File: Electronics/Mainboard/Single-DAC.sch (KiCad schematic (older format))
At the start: 21 parts, among them U10 AD8675, U5 AD5781, U9 AD8676xR

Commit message: Mainboard layout and schematic done
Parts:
- C26, C71, C72: LCSC (none) -> C1634
- C26, C27, C29, C30, C31, C32, C37: LCSC (none) -> C14663
- C32, C35, C36, C39, C40, C43, C44: LCSC (none) -> C15850
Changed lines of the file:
@@
 $Descr A4 11693 8268
 encoding utf-8
-Sheet 6 11
+Sheet 10 11
 Title ""
 Date ""
@@
 F 2 "Capacitor_SMD:C_0603_1608Metric_Pad1.05x0.95mm_HandSolder" H 6238 3350 50  0001 C CNN
 F 3 "~" H 6200 3500 50  0001 C CNN
+F 4 "C1634" H 6200 3500 50  0001 C CNN "LCSC"
 	1    6200 3500
 	1    0    0    -1
@@
 F 2 "Capacitor_SMD:C_0805_2012Metric_Pad1.15x1.40mm_HandSolder" H 9388 3950 50  0001 C CNN
 F 3 "~" H 9350 4100 50  0001 C CNN
+F 4 "C15850" H 9350 4100 50  0001 C CNN "LCSC"
 	1    9350 4100
 	1    0    0    -1
@@
 F 2 "Capacitor_SMD:C_0603_1608Metric_Pad1.05x0.95mm_HandSolder" H 8488 1950 50  0001 C CNN
 F 3 "~" H 8450 2100 50  0001 C CNN
+F 4 "C14663" H 8450 2100 50  0001 C CNN "LCSC"
 	1    8450 2100
 	1    0    0    -1
@@
 F 2 "Capacitor_SMD:C_0805_2012Metric_Pad1.15x1.40mm_HandSolder" H 8238 1950 50  0001 C CNN
 F 3 "~" H 8200 2100 50  0001 C CNN
+F 4 "C15850" H 8200 2100 50  0001 C CNN "LCSC"
 	1    8200 2100
 	1    0    0    -1
@@
 F 2 "Capacitor_SMD:C_0805_2012Metric_Pad1.15x1.40mm_HandSolder" H 8238 2450 50  0001 C CNN
 F 3 "~" H 8200 2600 50  0001 C CNN
+F 4 "C15850" H 8200 2600 50  0001 C CNN "LCSC"
 	1    8200 2600
 	1    0    0    -1
@@
 F 2 "Capacitor_SMD:C_0805_2012Metric_Pad1.15x1.40mm_HandSolder" H 8738 1950 50  0001 C CNN
 F 3 "~" H 8700 2100 50  0001 C CNN
+F 4 "C15850" H 8700 2100 50  0001 C CNN "LCSC"
 	1    8700 2100
 	1    0    0    -1
@@
 F 2 "Capacitor_SMD:C_0805_2012Metric_Pad1.15x1.40mm_HandSolder" H 8738 2450 50  0001 C CNN
 F 3 "~" H 8700 2600 50  0001 C CNN
+F 4 "C15850" H 8700 2600 50  0001 C CNN "LCSC"
 	1    8700 2600
 	1    0    0    -1
@@
 F 2 "Capacitor_SMD:C_0805_2012Metric_Pad1.15x1.40mm_HandSolder" H 9238 1950 50  0001 C CNN
 F 3 "~" H 9200 2100 50  0001 C CNN
+F 4 "C15850" H 9200 2100 50  0001 C CNN "LCSC"
 	1    9200 2100
 	1    0    0    -1
@@
 F 2 "Capacitor_SMD:C_0805_2012Metric_Pad1.15x1.40mm_HandSolder" H 9238 2450 50  0001 C CNN
 F 3 "~" H 9200 2600 50  0001 C CNN
+F 4 "C15850" H 9200 2600 50  0001 C CNN "LCSC"
 	1    9200 2600
 	1    0    0    -1
@@
 F 2 "Capacitor_SMD:C_0603_1608Metric_Pad1.05x0.95mm_HandSolder" H 8488 2450 50  0001 C CNN
 F 3 "~" H 8450 2600 50  0001 C CNN
+F 4 "C14663" H 8450 2600 50  0001 C CNN "LCSC"
 	1    8450 2600
 	1    0    0    -1
@@
 F 2 "Capacitor_SMD:C_0603_1608Metric_Pad1.05x0.95mm_HandSolder" H 8988 2450 50  0001 C CNN
 F 3 "~" H 8950 2600 50  0001 C CNN
+F 4 "C14663" H 8950 2600 50  0001 C CNN "LCSC"
 	1    8950 2600
 	1    0    0    -1
@@
 F 2 "Capacitor_SMD:C_0603_1608Metric_Pad1.05x0.95mm_HandSolder" H 8988 1950 50  0001 C CNN
 F 3 "~" H 8950 2100 50  0001 C CNN
+F 4 "C14663" H 8950 2100 50  0001 C CNN "LCSC"
 	1    8950 2100
 	1    0    0    -1
@@
 F 2 "Capacitor_SMD:C_0603_1608Metric_Pad1.05x0.95mm_HandSolder" H 9488 1950 50  0001 C CNN
 F 3 "~" H 9450 2100 50  0001 C CNN
+F 4 "C14663" H 9450 2100 50  0001 C CNN "LCSC"
 	1    9450 2100
 	1    0    0    -1
@@
 F 2 "Capacitor_SMD:C_0603_1608Metric_Pad1.05x0.95mm_HandSolder" H 9488 2450 50  0001 C CNN
 F 3 "~" H 9450 2600 50  0001 C CNN
+F 4 "C14663" H 9450 2600 50  0001 C CNN "LCSC"
 	1    9450 2600
 	1    0    0    -1
@@
 F 2 "Capacitor_SMD:C_0603_1608Metric_Pad1.05x0.95mm_HandSolder" H 9638 3950 50  0001 C CNN
 F 3 "~" H 9600 4100 50  0001 C CNN
+F 4 "C14663" H 9600 4100 50  0001 C CNN "LCSC"
 	1    9600 4100
 	1    0    0    -1
@@
 F 2 "Capacitor_SMD:C_0603_1608Metric_Pad1.05x0.95mm_HandSolder" H 4838 2150 50  0001 C CNN
 F 3 "~" H 4800 2300 50  0001 C CNN
+F 4 "C1634" H 4800 2300 50  0001 C CNN "LCSC"
 	1    4800 2300
 	1    0    0    -1
@@
 F 2 "Capacitor_SMD:C_0603_1608Metric_Pad1.05x0.95mm_HandSolder" H 4838 5000 50  0001 C CNN
 F 3 "~" H 4800 5150 50  0001 C CNN
+F 4 "C1634" H 4800 5150 50  0001 C CNN "LCSC"
 	1    4800 5150
 	1    0    0    -1

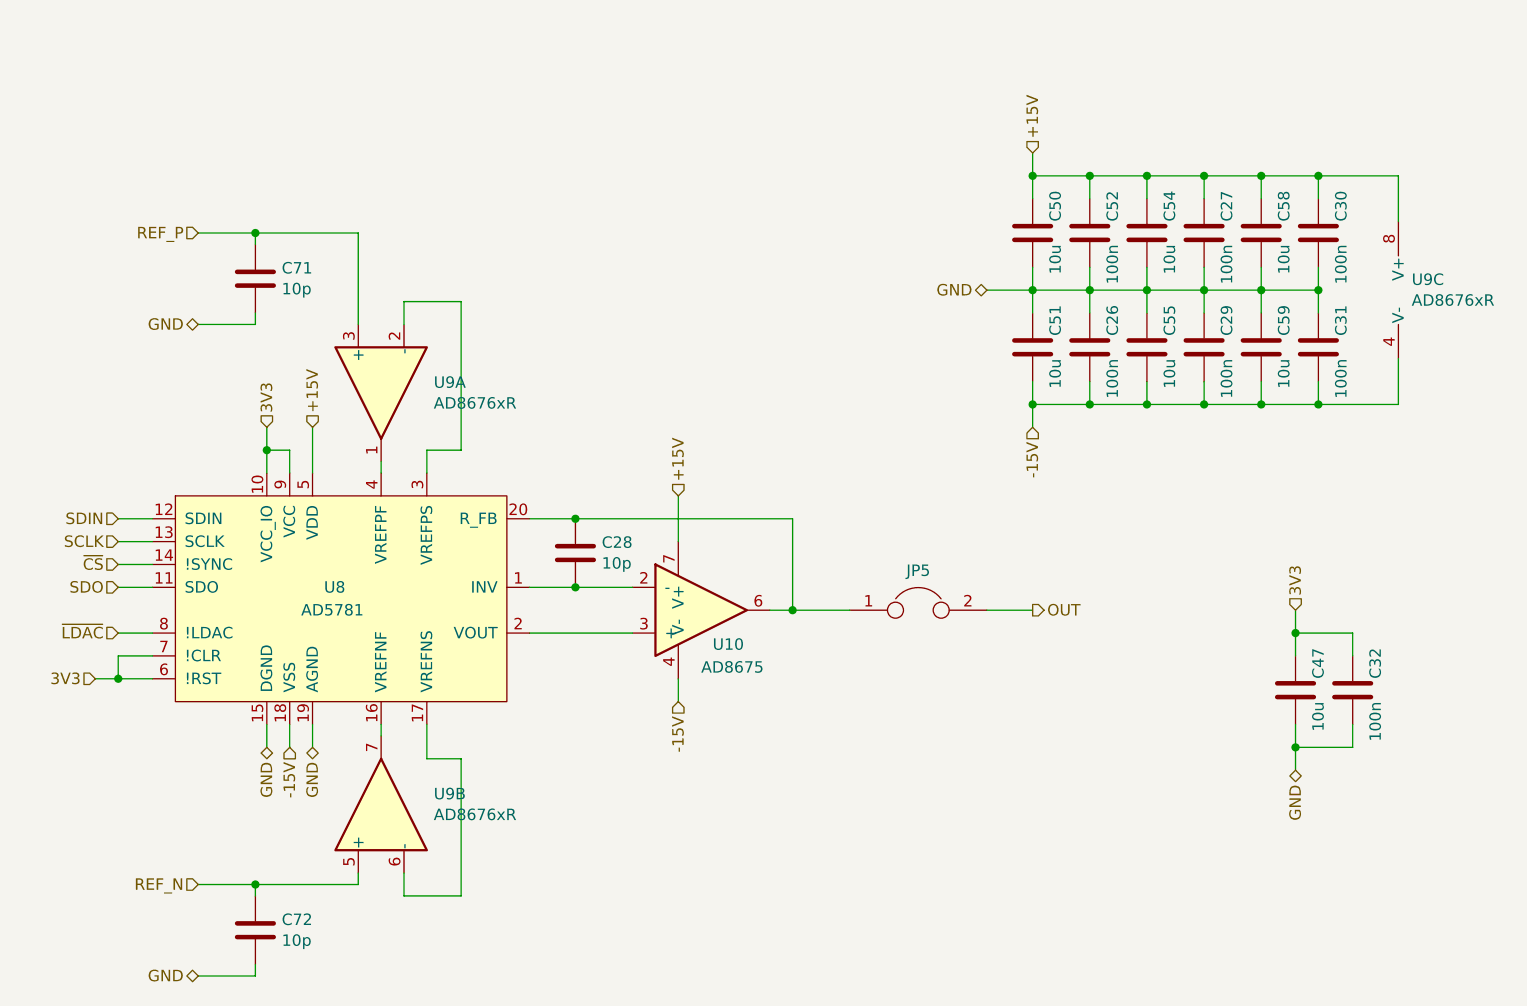
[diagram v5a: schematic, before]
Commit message: Added images
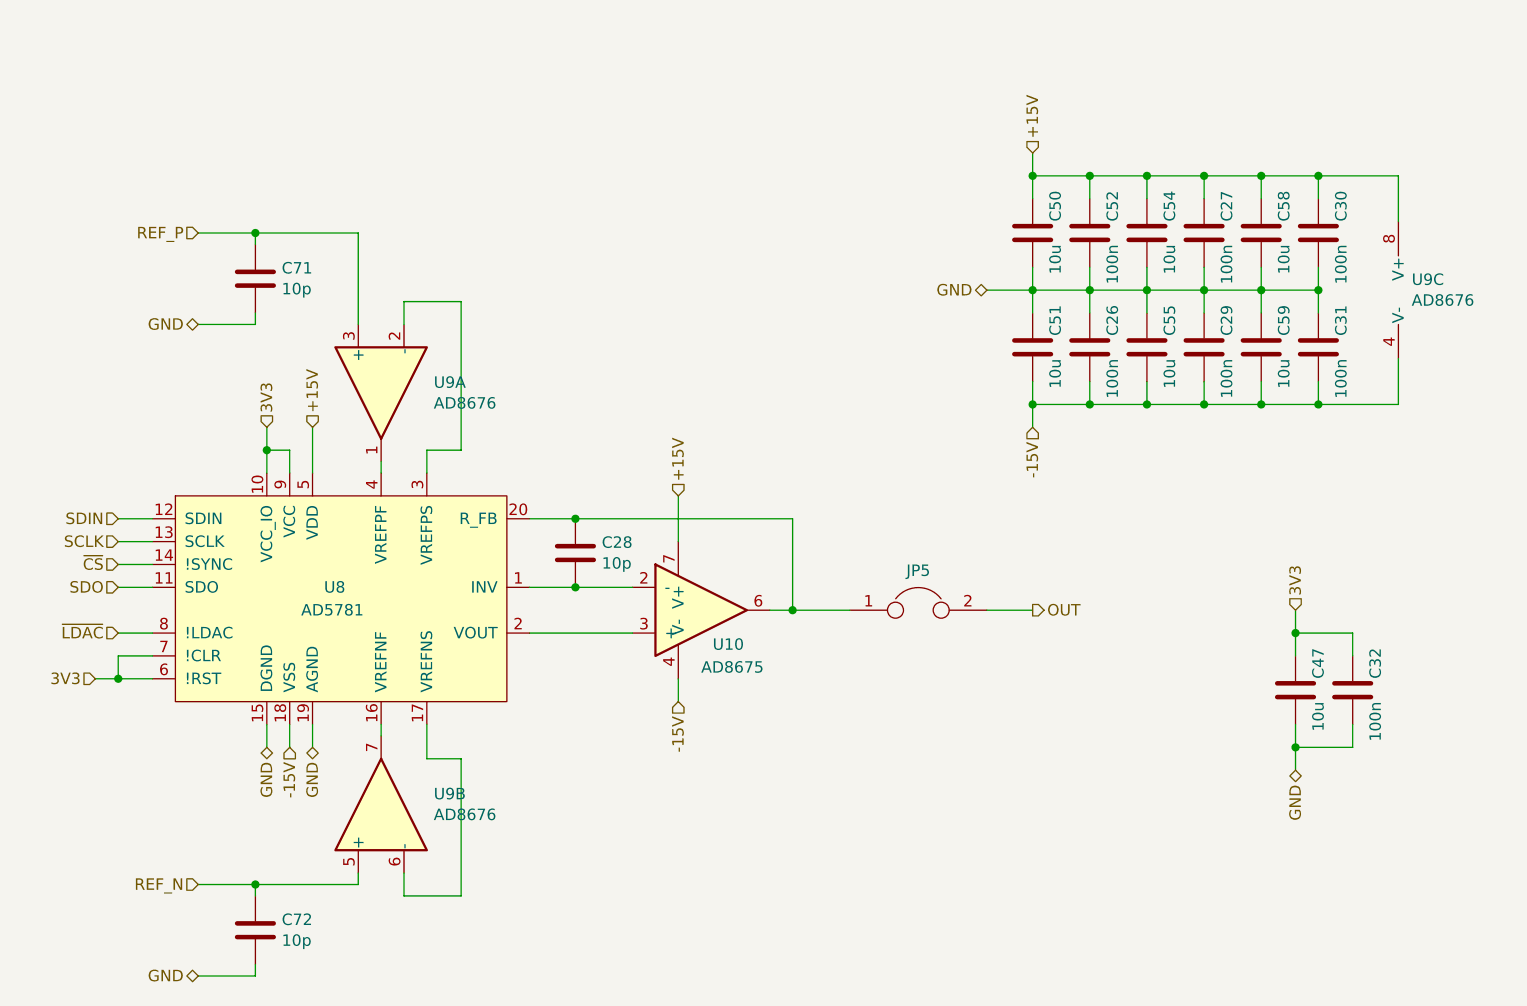
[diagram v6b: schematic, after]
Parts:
- U10: Digikey (none) -> AD8675ARZ-REEL7CT-ND
- U5: Digikey (none) -> AD5781ARUZ-ND
- U9: value AD8676xR -> AD8676; Digikey (none) -> AD8676ARZ-ND
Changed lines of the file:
@@
 $Descr A4 11693 8268
 encoding utf-8
-Sheet 10 11
+Sheet 9 11
 Title ""
 Date ""
@@
 F 2 "Package_SO:TSSOP-20_4.4x6.5mm_P0.65mm" H 4550 3800 50  0001 C CNN
 F 3 "" H 4550 3800 50  0001 C CNN
+F 4 "AD5781ARUZ-ND " H 5150 3750 50  0001 C CNN "Digikey"
 	1    5150 3750
 	1    0    0    -1
@@
 AR Path="/5F11EDFC/5EBF2A39" Ref="U17"  Part="1"
 F 0 "U9" V 5304 2570 50  0000 R CNN
-F 1 "AD8676xR" V 5395 2570 50  0000 R CNN
+F 1 "AD8676" V 5395 2570 50  0000 R CNN
 F 2 "Package_SO:SOIC-8_3.9x4.9mm_P1.27mm" H 5450 2800 50  0001 C CNN
 F 3 "https://www.analog.com/media/en/technical-documentation/data-sheets/AD8676.pdf" H 5600 2950 50  0001 C CNN
+F 4 "AD8676ARZ-ND " H 5350 2800 50  0001 C CNN "Digikey"
 	1    5350 2800
 	0    -1   1    0
@@
 AR Path="/5F11EDFC/5EBF3E04" Ref="U17"  Part="3"
 F 0 "U9" H 9858 2396 50  0000 L CNN
-F 1 "AD8676xR" H 9858 2305 50  0000 L CNN
+F 1 "AD8676" H 9858 2305 50  0000 L CNN
 F 2 "Package_SO:SOIC-8_3.9x4.9mm_P1.27mm" H 9900 2350 50  0001 C CNN
 F 3 "https://www.analog.com/media/en/technical-documentation/data-sheets/AD8676.pdf" H 10050 2500 50  0001 C CNN
+F 4 "AD8676ARZ-ND " H 9800 2350 50  0001 C CNN "Digikey"
 	3    9800 2350
 	1    0    0    -1
@@
 F 2 "Package_SO:SOIC-8_3.9x4.9mm_P1.27mm" H 6950 4000 50  0001 C CNN
 F 3 "" H 6950 4000 50  0001 C CNN
+F 4 "AD8675ARZ-REEL7CT-ND " H 6750 3750 50  0001 C CNN "Digikey"
 	1    6750 3750
 	1    0    0    -1
@@
 AR Path="/5F11EDFC/5EBF327E" Ref="U17"  Part="2"
 F 0 "U9" V 5396 4370 50  0000 R CNN
-F 1 "AD8676xR" V 5305 4370 50  0000 R CNN
+F 1 "AD8676" V 5305 4370 50  0000 R CNN
 F 2 "Package_SO:SOIC-8_3.9x4.9mm_P1.27mm" H 5450 4600 50  0001 C CNN
 F 3 "https://www.analog.com/media/en/technical-documentation/data-sheets/AD8676.pdf" H 5600 4750 50  0001 C CNN
+F 4 "AD8676ARZ-ND " H 5350 4600 50  0001 C CNN "Digikey"
 	2    5350 4600
 	0    -1   -1   0
